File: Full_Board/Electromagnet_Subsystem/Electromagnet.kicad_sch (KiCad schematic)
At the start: 3 parts, among them IC5 DRV8210DRLR

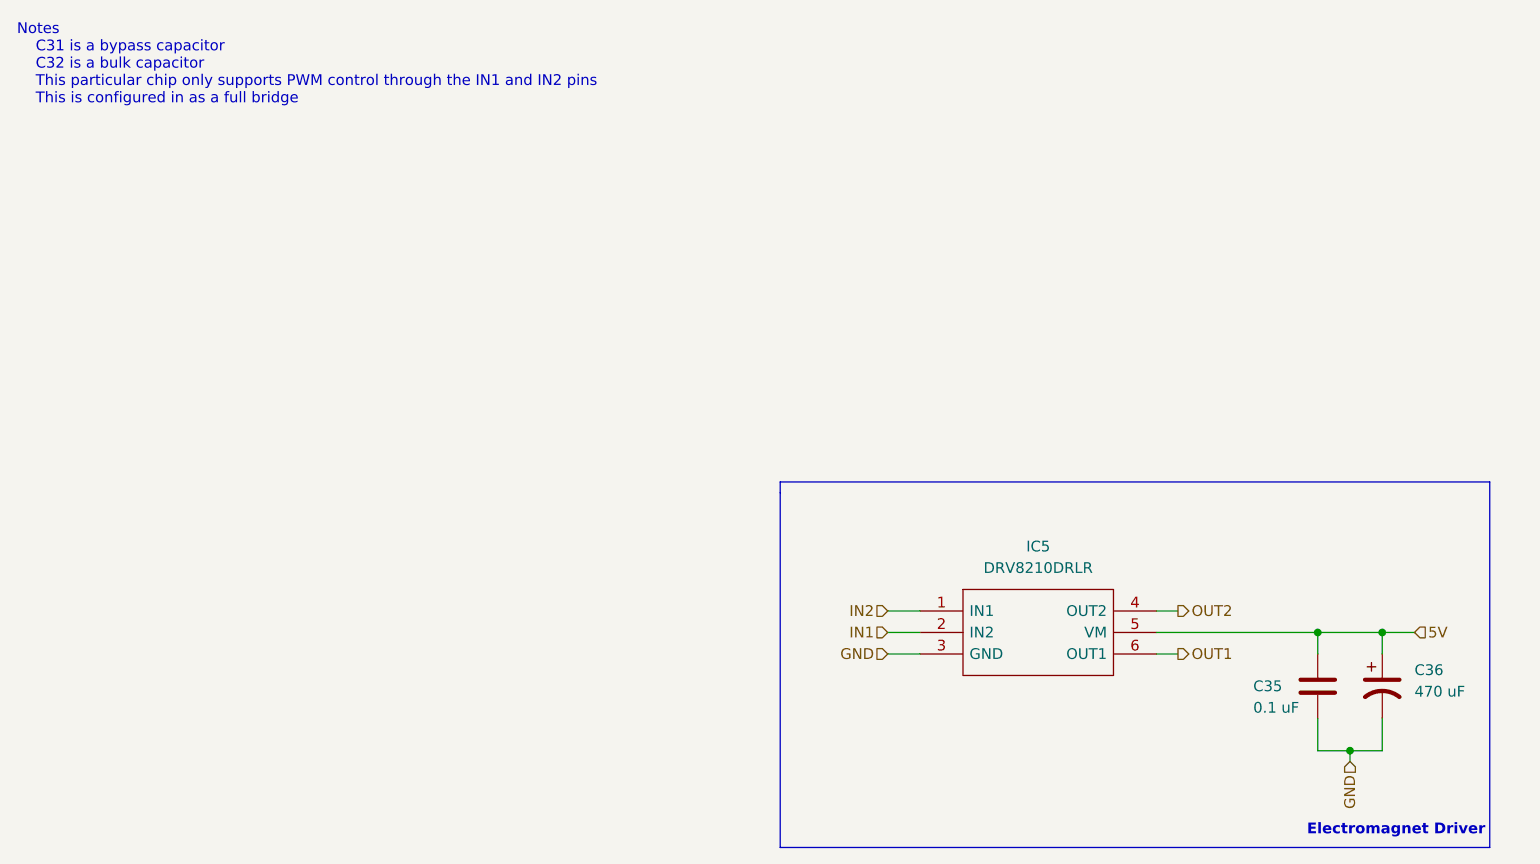
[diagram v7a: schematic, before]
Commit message: Replaced electromagnet IC and fixed ERC errors with stepper driver
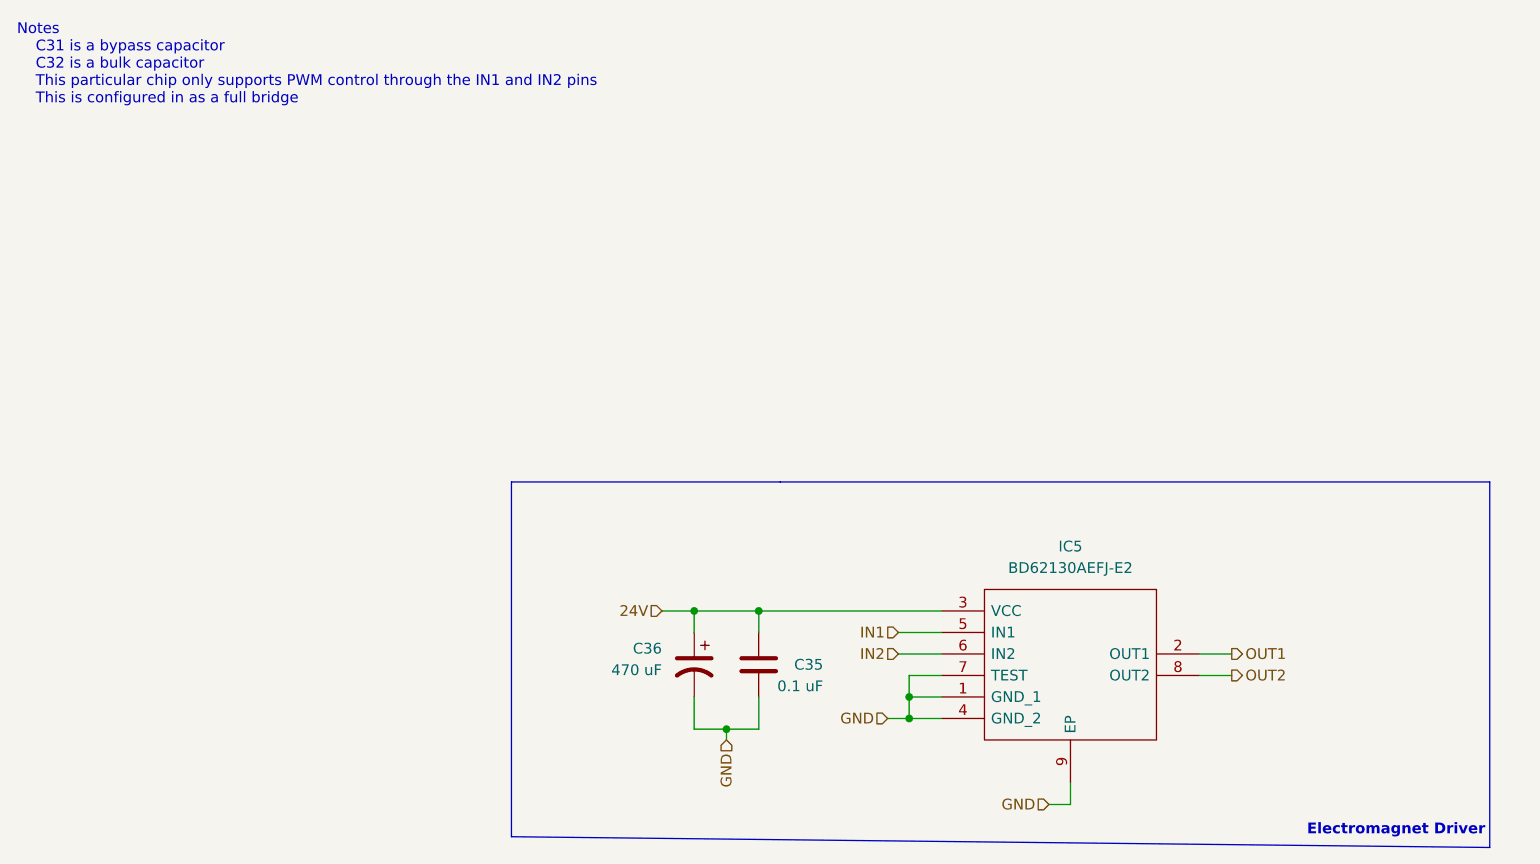
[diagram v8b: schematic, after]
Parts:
- removed IC5: DRV8210DRLR, SOTFL50P160X60-6N, symbol DRV8210DRLR:DRV8210DRLR
- added IC5: BD62130AEFJ-E2, SOIC127P600X100-9N, symbol BD62130AEFJ-E2:BD62130AEFJ-E2
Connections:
- net GND: now also IC5.1 (GND_1), IC5.4 (GND_2), IC5.7 (TEST), IC5.9 (EP)
- net IN1: now also IC5.5 (IN1)
- net IN2: now also IC5.6 (IN2)
- net OUT1: now also IC5.2 (OUT1)
- net OUT2: now also IC5.8 (OUT2)
- net 5V renamed 24V
- net 24V: now also IC5.3 (VCC)
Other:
- moved on the sheet: C35, C36
